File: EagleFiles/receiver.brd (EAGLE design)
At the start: 100 x 80 mm, 3 parts, among them IC1 MEGA8-AI

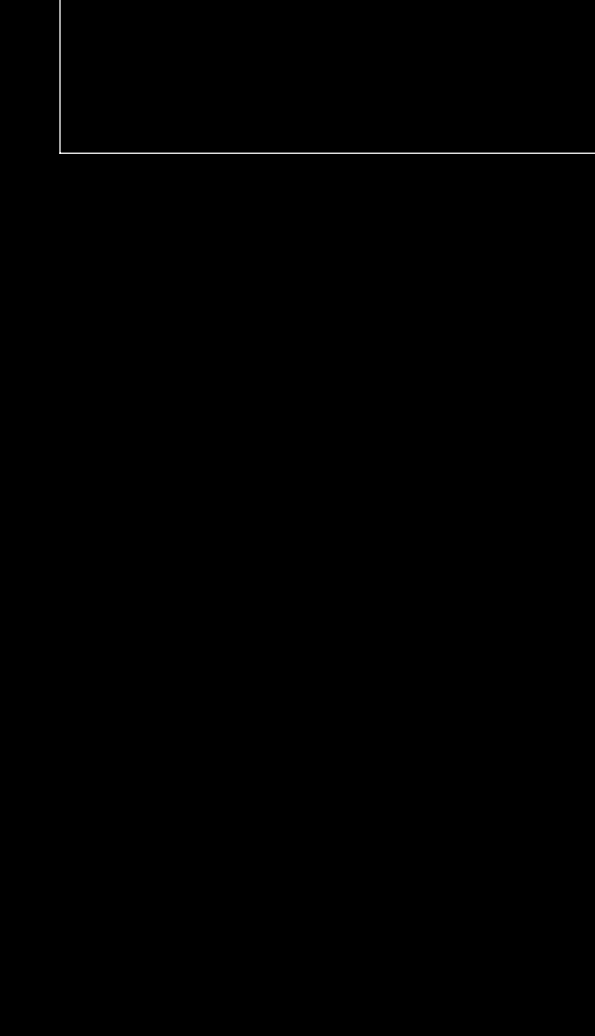
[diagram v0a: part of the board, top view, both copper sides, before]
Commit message: Added eagle files for LB1836M breakout board and unfinished receiver
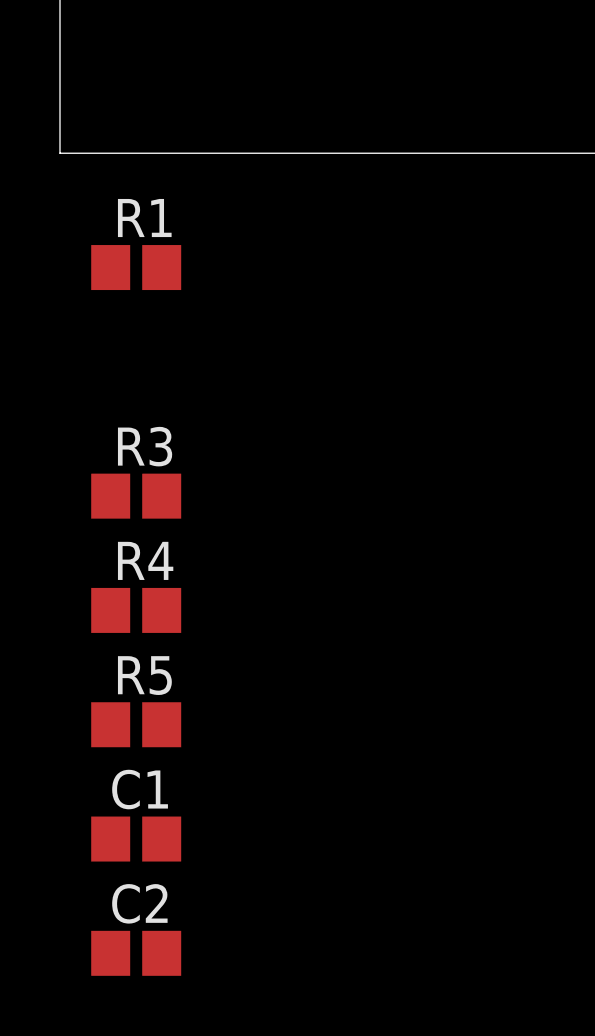
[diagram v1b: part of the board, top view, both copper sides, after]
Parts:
- added C1, C2: (no value), resistor:C0805
- added R1, R3, R4, R5: (no value), resistor:R2012
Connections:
- removed net AVCC: IC1.18
- new net ANT: RFM12B.ANT
- new net N$1: IC1.16, RFM12B.SDO
- new net N$10: LB1836M.IN3, R5.1
- new net N$11: IC1.24, R3.1
- new net N$12: IC1.25, R4.2
- new net N$13: IC1.26, R5.2
- new net N$2: IC1.15, RFM12B.SDI
- new net N$3: IC1.17, RFM12B.SCK
- new net N$4: IC1.14, RFM12B.NSEL
- new net N$5: IC1.32, RFM12B.NIRQ
- new net N$6: LB1836M.IN1, R1.2
- new net N$7: IC1.23, R1.1
- new net N$8: LB1836M.IN2, R3.2
- new net N$9: LB1836M.IN4, R4.1
- net GND: now also C1.1, C2.1, LB1836M.GN2, LB1836M.GND1, RFM12B.GND1, RFM12B.GND2
- net VCC: now also C1.2, IC1.18, LB1836M.VCC, LB1836M.VS1, LB1836M.VS2, RFM12B.VDD
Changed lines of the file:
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@@
 <element name="LB1836M" library="jeroen" package="MFP-14" value="LB1836M" x="35.56" y="44.45"/>
 <element name="RFM12B" library="jeroen" package="RFM12B" value="RFM12B" x="41.91" y="62.23"/>
+<element name="R1" library="resistor" package="R2012" value="" x="2.54" y="-3.81"/>
+<element name="R3" library="resistor" package="R2012" value="" x="2.54" y="-11.43"/>
+<element name="R4" library="resistor" package="R2012" value="" x="2.54" y="-15.24"/>
+<element name="R5" library="resistor" package="R2012" value="" x="2.54" y="-19.05"/>
+<element name="C1" library="resistor" package="C0805" value="" x="2.54" y="-22.86"/>
+<element name="C2" library="resistor" package="C0805" value="" x="2.54" y="-26.67"/>
 </elements>
 <signals>
 <signal name="GND">
+<contactref element="RFM12B" pad="GND2"/>
+<contactref element="RFM12B" pad="GND1"/>
 <contactref element="IC1" pad="3"/>
 <contactref element="IC1" pad="5"/>
+<contactref element="IC1" pad="5"/>
 <contactref element="IC1" pad="21"/>
-<wire x1="52.8574" y1="48.19" x2="52.8574" y2="46.59" width="0" layer="19" extent="1-1"/>
-<wire x1="61.4426" y1="47.39" x2="52.8574" y2="46.59" width="0" layer="19" extent="1-1"/>
+<contactref element="LB1836M" pad="GND1"/>
+<contactref element="LB1836M" pad="GN2"/>
+<contactref element="C1" pad="1"/>
+<contactref element="C2" pad="1"/>
+<wire x1="52.8574" y1="48.19" x2="49.91" y2="60.23" width="0" layer="19" extent="1-1"/>
+<wire x1="52.8574" y1="46.59" x2="52.8574" y2="48.19" width="0" layer="19" extent="1-1"/>
+<wire x1="61.4426" y1="47.39" x2="52.8574" y2="48.19" width="0" layer="19" extent="1-1"/>
+<wire x1="38.36" y1="47.45" x2="52.8574" y2="48.19" width="0" layer="19" extent="1-1"/>
+<wire x1="32.76" y1="41.45" x2="38.36" y2="47.45" width="0" layer="19" extent="1-1"/>
+<wire x1="33.91" y1="56.23" x2="38.36" y2="47.45" width="0" layer="19" extent="1-1"/>
+<wire x1="1.69" y1="-22.86" x2="32.76" y2="41.45" width="0" layer="19" extent="1-1"/>
+<wire x1="1.69" y1="-26.67" x2="1.69" y2="-22.86" width="0" layer="19" extent="1-1"/>
+</signal>
+<signal name="N$1">
+<contactref element="RFM12B" pad="SDO"/>
+<contactref element="IC1" pad="16"/>
+<wire x1="59.95" y1="42.6974" x2="33.91" y2="68.23" width="0" layer="19" extent="1-1"/>
+</signal>
+<signal name="N$2">
+<contactref element="RFM12B" pad="SDI"/>
+<contactref element="IC1" pad="15"/>
+<wire x1="59.15" y1="42.6974" x2="49.91" y2="64.23" width="0" layer="19" extent="1-1"/>
+</signal>
+<signal name="N$4">
+<contactref element="RFM12B" pad="NSEL"/>
+<contactref element="IC1" pad="14"/>
+<wire x1="58.35" y1="42.6974" x2="49.91" y2="68.23" width="0" layer="19" extent="1-1"/>
 </signal>
 <signal name="VCC">
 <contactref element="IC1" pad="4"/>
 <contactref element="IC1" pad="6"/>
-<wire x1="52.8574" y1="47.39" x2="52.8574" y2="45.79" width="0" layer="19" extent="1-1"/>
+<contactref element="RFM12B" pad="VDD"/>
+<contactref element="IC1" pad="18"/>
+<contactref element="LB1836M" pad="VCC"/>
+<contactref element="LB1836M" pad="VS1"/>
+<contactref element="LB1836M" pad="VS2"/>
+<contactref element="C1" pad="2"/>
+<wire x1="52.8574" y1="47.39" x2="49.91" y2="58.23" width="0" layer="19" extent="1-1"/>
+<wire x1="52.8574" y1="45.79" x2="52.8574" y2="47.39" width="0" layer="19" extent="1-1"/>
+<wire x1="61.4426" y1="44.99" x2="52.8574" y2="45.79" width="0" layer="19" extent="1-1"/>
+<wire x1="38.36" y1="44.45" x2="52.8574" y2="45.79" width="0" layer="19" extent="1-1"/>
+<wire x1="32.76" y1="44.45" x2="38.36" y2="44.45" width="0" layer="19" extent="1-1"/>
+<wire x1="32.76" y1="47.45" x2="32.76" y2="44.45" width="0" layer="19" extent="1-1"/>
+<wire x1="3.39" y1="-22.86" x2="32.76" y2="44.45" width="0" layer="19" extent="1-1"/>
 </signal>
-<signal name="AVCC">
-<contactref element="IC1" pad="18"/>
+<signal name="N$3">
+<contactref element="RFM12B" pad="SCK"/>
+<contactref element="IC1" pad="17"/>
+<wire x1="61.4426" y1="44.19" x2="49.91" y2="66.23" width="0" layer="19" extent="1-1"/>
+</signal>
+<signal name="ANT">
+<contactref element="RFM12B" pad="ANT"/>
+</signal>
+<signal name="N$5">
+<contactref element="IC1" pad="32"/>
+<contactref element="RFM12B" pad="NIRQ"/>
+<wire x1="33.91" y1="66.23" x2="54.35" y2="51.2826" width="0" layer="19" extent="1-1"/>
+</signal>
+<signal name="N$6">
+<contactref element="LB1836M" pad="IN1"/>
+<contactref element="R1" pad="2"/>
+<wire x1="3.39" y1="-3.81" x2="32.76" y2="46.45" width="0" layer="19" extent="1-1"/>
+</signal>
+<signal name="N$8">
+<contactref element="LB1836M" pad="IN2"/>
+<contactref element="R3" pad="2"/>
+<wire x1="3.39" y1="-11.43" x2="32.76" y2="42.45" width="0" layer="19" extent="1-1"/>
+</signal>
+<signal name="N$9">
+<contactref element="LB1836M" pad="IN4"/>
+<contactref element="R4" pad="1"/>
+<wire x1="1.69" y1="-15.24" x2="38.36" y2="42.45" width="0" layer="19" extent="1-1"/>
+</signal>
+<signal name="N$10">
+<contactref element="LB1836M" pad="IN3"/>
+<contactref element="R5" pad="1"/>
+<wire x1="1.69" y1="-19.05" x2="38.36" y2="46.45" width="0" layer="19" extent="1-1"/>
+</signal>
+<signal name="N$7">
+<contactref element="R1" pad="1"/>
+<contactref element="IC1" pad="23"/>
+<wire x1="1.69" y1="-3.81" x2="61.4426" y2="48.99" width="0" layer="19" extent="1-1"/>
+</signal>
+<signal name="N$11">
+<contactref element="R3" pad="1"/>
+<contactref element="IC1" pad="24"/>
+<wire x1="1.69" y1="-11.43" x2="61.4426" y2="49.79" width="0" layer="19" extent="1-1"/>
+</signal>
+<signal name="N$12">
+<contactref element="R4" pad="2"/>
+<contactref element="IC1" pad="25"/>
+<wire x1="3.39" y1="-15.24" x2="59.95" y2="51.2826" width="0" layer="19" extent="1-1"/>
+</signal>
+<signal name="N$13">
+<contactref element="R5" pad="2"/>
+<contactref element="IC1" pad="26"/>
+<wire x1="3.39" y1="-19.05" x2="59.15" y2="51.2826" width="0" layer="19" extent="1-1"/>
 </signal>
 </signals>
